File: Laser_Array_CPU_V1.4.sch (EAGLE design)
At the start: 71 parts, among them IC1 PIC24FJ64GA004, J1 MA16-2, J3 22-23-2021, J4 22-23-2021, J8 22-23-2021, U1 MAX6817, U2 LP2985-28DBVTE4, U4 LP2985-50DBVR, X1 22-23-2031, X2 22-23-2041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

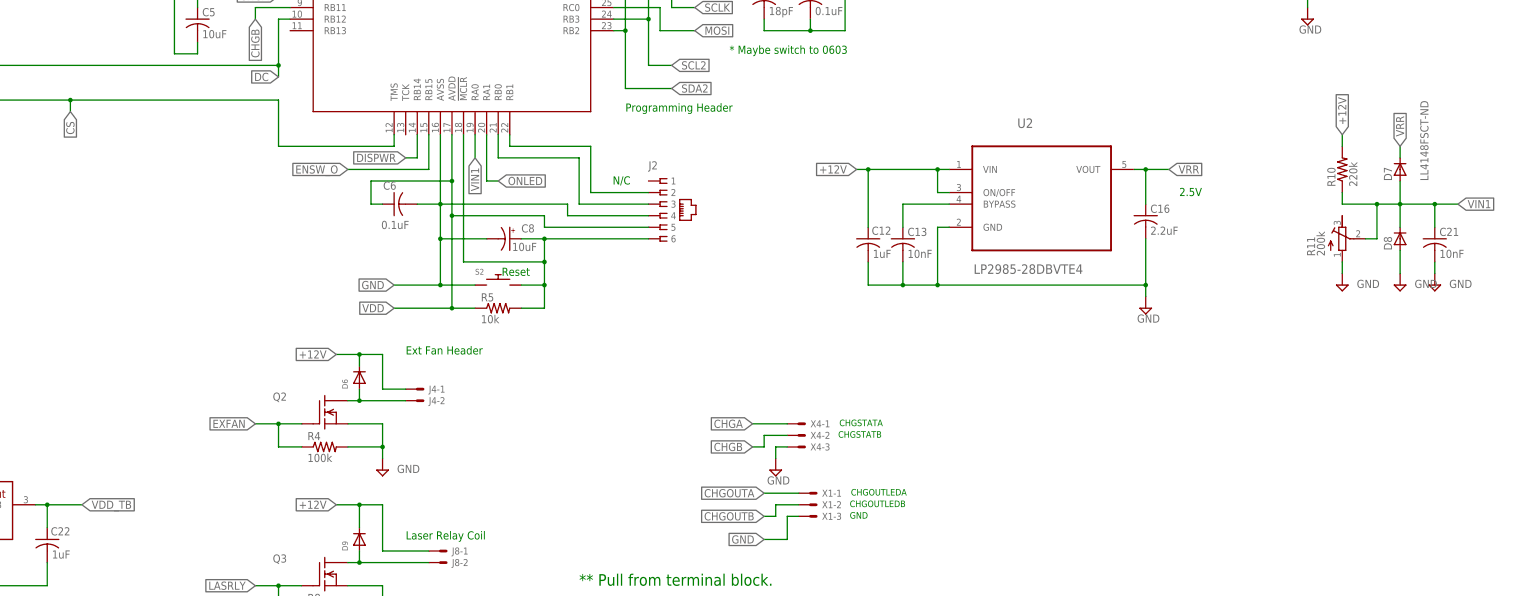
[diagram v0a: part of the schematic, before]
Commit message: Finished Laser_Array next versions, all three boards including revised charger board
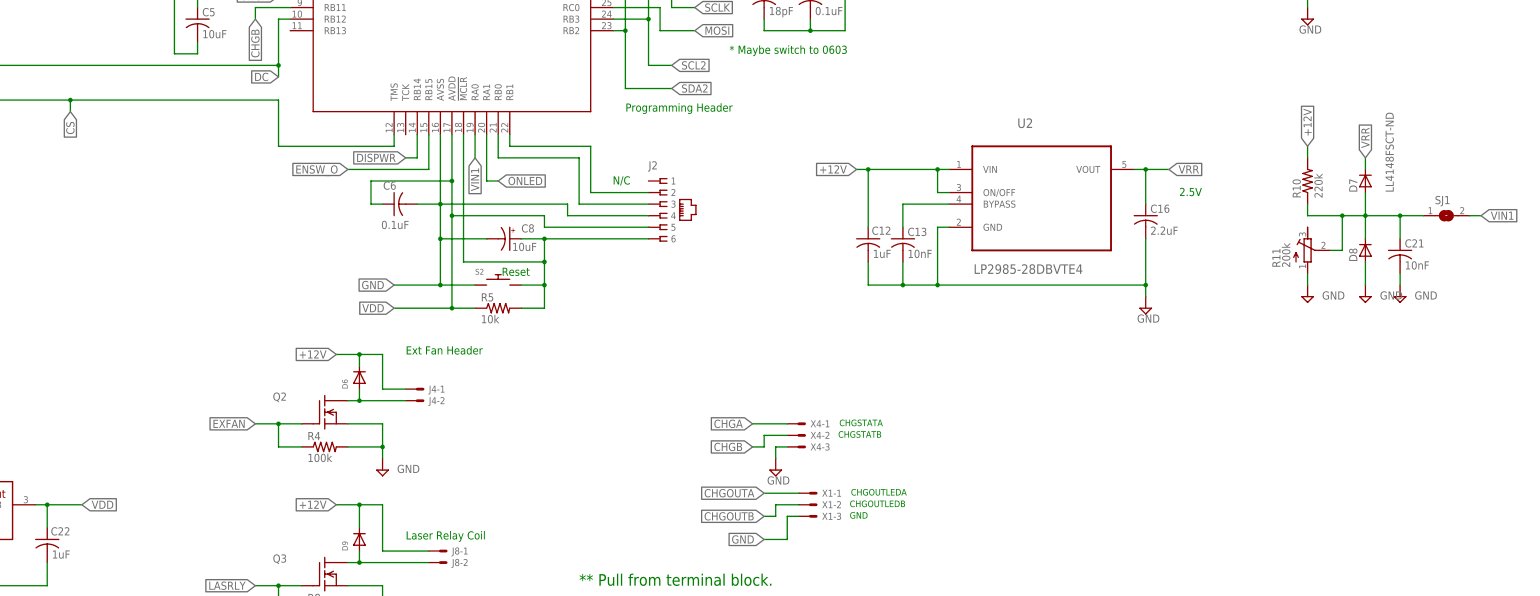
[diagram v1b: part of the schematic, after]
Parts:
- added SJ1: (no value), jumper:SJ
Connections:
- removed net N$3: C22.1, U3.P$3
- net VDD: now also C22.1, U3.P$3
- net VIN1: now also SJ1.1, SJ1.2
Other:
- moved on the sheet: C21, D7, D8, R10, R11
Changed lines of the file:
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@@
 </variantdefs>
 <classes>
-<class number="0" name="default" width="0.254" drill="0.508">
+<class number="0" name="default" width="0.1016" drill="0.508">
 <clearance class="0" value="0.2032"/>
 </class>
@@
 <part name="C23" library="rcl" deviceset="C-US" device="C0805" value="4.7uF"/>
 <part name="SUPPLY6" library="supply2" deviceset="GND" device=""/>
+<part name="SJ1" library="jumper" deviceset="SJ" device=""/>
 </parts>
 <sheets>
@@
 <attribute name="VALUE" x="168.656" y="-1.651" size="1.778" layer="96"/>
 </instance>
-<instance part="R10" gate="G$1" x="210.82" y="12.7" smashed="yes" rot="R90">
-<attribute name="NAME" x="209.3214" y="8.89" size="1.778" layer="95" rot="R90"/>
-<attribute name="VALUE" x="214.122" y="8.89" size="1.778" layer="96" rot="R90"/>
-</instance>
-<instance part="SUPPLY9" gate="GND" x="210.82" y="-12.7" smashed="yes">
-<attribute name="VALUE" x="213.995" y="-13.335" size="1.778" layer="96"/>
-</instance>
-<instance part="C21" gate="G$1" x="231.14" y="-2.54" smashed="yes">
-<attribute name="NAME" x="232.156" y="-1.905" size="1.778" layer="95"/>
-<attribute name="VALUE" x="232.156" y="-6.731" size="1.778" layer="96"/>
-</instance>
-<instance part="SUPPLY12" gate="GND" x="231.14" y="-12.7" smashed="yes">
-<attribute name="VALUE" x="234.315" y="-13.335" size="1.778" layer="96"/>
-</instance>
-<instance part="D7" gate="G$1" x="223.52" y="12.7" smashed="yes" rot="R90">
-<attribute name="NAME" x="221.742" y="10.16" size="1.778" layer="95" rot="R90"/>
-<attribute name="VALUE" x="229.743" y="10.16" size="1.778" layer="96" rot="R90"/>
-</instance>
-<instance part="D8" gate="G$1" x="223.52" y="-2.54" smashed="yes" rot="R90">
-<attribute name="NAME" x="221.742" y="-5.08" size="1.778" layer="95" rot="R90"/>
-</instance>
-<instance part="SUPPLY10" gate="GND" x="223.52" y="-12.7" smashed="yes">
-<attribute name="VALUE" x="226.695" y="-13.335" size="1.778" layer="96"/>
-</instance>
-<instance part="R11" gate="G$1" x="210.82" y="-2.54"/>
+<instance part="R10" gate="G$1" x="203.2" y="10.16" smashed="yes" rot="R90">
+<attribute name="NAME" x="201.7014" y="6.35" size="1.778" layer="95" rot="R90"/>
+<attribute name="VALUE" x="206.502" y="6.35" size="1.778" layer="96" rot="R90"/>
+</instance>
+<instance part="SUPPLY9" gate="GND" x="203.2" y="-15.24" smashed="yes">
+<attribute name="VALUE" x="206.375" y="-15.875" size="1.778" layer="96"/>
+</instance>
+<instance part="C21" gate="G$1" x="223.52" y="-5.08" smashed="yes">
+<attribute name="NAME" x="224.536" y="-4.445" size="1.778" layer="95"/>
+<attribute name="VALUE" x="224.536" y="-9.271" size="1.778" layer="96"/>
+</instance>
+<instance part="SUPPLY12" gate="GND" x="223.52" y="-15.24" smashed="yes">
+<attribute name="VALUE" x="226.695" y="-15.875" size="1.778" layer="96"/>
+</instance>
+<instance part="D7" gate="G$1" x="215.9" y="10.16" smashed="yes" rot="R90">
+<attribute name="NAME" x="214.122" y="7.62" size="1.778" layer="95" rot="R90"/>
+<attribute name="VALUE" x="222.123" y="7.62" size="1.778" layer="96" rot="R90"/>
+</instance>
+<instance part="D8" gate="G$1" x="215.9" y="-5.08" smashed="yes" rot="R90">
+<attribute name="NAME" x="214.122" y="-7.62" size="1.778" layer="95" rot="R90"/>
+</instance>
+<instance part="SUPPLY10" gate="GND" x="215.9" y="-15.24" smashed="yes">
+<attribute name="VALUE" x="219.075" y="-15.875" size="1.778" layer="96"/>
+</instance>
+<instance part="R11" gate="G$1" x="203.2" y="-5.08"/>
 <instance part="R13" gate="G$1" x="200.66" y="76.2" smashed="yes" rot="R90">
 <attribute name="NAME" x="199.1614" y="72.39" size="1.778" layer="95" rot="R90"/>
@@
 </instance>
 <instance part="SUPPLY6" gate="GND" x="-88.9" y="-86.36"/>
+<instance part="SJ1" gate="1" x="233.68" y="2.54"/>
 </instances>
 <busses>
@@
 <wire x1="-139.7" y1="78.74" x2="-134.62" y2="78.74" width="0.1524" layer="91"/>
 </segment>
+<segment>
+<pinref part="U3" gate="G$1" pin="P$3"/>
+<wire x1="-76.2" y1="-60.96" x2="-73.66" y2="-60.96" width="0.1524" layer="91"/>
+<pinref part="C22" gate="G$1" pin="1"/>
+<wire x1="-73.66" y1="-60.96" x2="-66.04" y2="-60.96" width="0.1524" layer="91"/>
+<wire x1="-73.66" y1="-66.04" x2="-73.66" y2="-60.96" width="0.1524" layer="91"/>
+<junction x="-73.66" y="-60.96"/>
+<label x="-66.04" y="-60.96" size="1.778" layer="95" xref="yes"/>
+</segment>
 </net>
 <net name="+12V" class="0">
@@
 <segment>
 <pinref part="R10" gate="G$1" pin="2"/>
-<wire x1="210.82" y1="17.78" x2="210.82" y2="20.32" width="0.1524" layer="91"/>
-<label x="210.82" y="20.32" size="1.778" layer="95" rot="R90" xref="yes"/>
+<wire x1="203.2" y1="15.24" x2="203.2" y2="17.78" width="0.1524" layer="91"/>
+<label x="203.2" y="17.78" size="1.778" layer="95" rot="R90" xref="yes"/>
 </segment>
 <segment>
@@
 <segment>
 <pinref part="SUPPLY9" gate="GND" pin="GND"/>
-<wire x1="210.82" y1="-7.62" x2="210.82" y2="-10.16" width="0.1524" layer="91"/>
+<wire x1="203.2" y1="-10.16" x2="203.2" y2="-12.7" width="0.1524" layer="91"/>
 <pinref part="R11" gate="G$1" pin="A"/>
 </segment>
@@
 <pinref part="SUPPLY12" gate="GND" pin="GND"/>
 <pinref part="C21" gate="G$1" pin="2"/>
-<wire x1="231.14" y1="-10.16" x2="231.14" y2="-7.62" width="0.1524" layer="91"/>
+<wire x1="223.52" y1="-12.7" x2="223.52" y2="-10.16" width="0.1524" layer="91"/>
 </segment>
 <segment>
 <pinref part="SUPPLY10" gate="GND" pin="GND"/>
 <pinref part="D8" gate="G$1" pin="A"/>
-<wire x1="223.52" y1="-10.16" x2="223.52" y2="-5.08" width="0.1524" layer="91"/>
+<wire x1="215.9" y1="-12.7" x2="215.9" y2="-7.62" width="0.1524" layer="91"/>
 </segment>
 <segment>
@@
 <segment>
 <pinref part="D7" gate="G$1" pin="C"/>
-<wire x1="223.52" y1="15.24" x2="223.52" y2="17.78" width="0.1524" layer="91"/>
-<label x="223.52" y="17.78" size="1.778" layer="95" rot="R90" xref="yes"/>
+<wire x1="215.9" y1="12.7" x2="215.9" y2="15.24" width="0.1524" layer="91"/>
+<label x="215.9" y="15.24" size="1.778" layer="95" rot="R90" xref="yes"/>
 </segment>
 </net>
@@
 <segment>
 <pinref part="R10" gate="G$1" pin="1"/>
-<wire x1="210.82" y1="7.62" x2="210.82" y2="5.08" width="0.1524" layer="91"/>
+<wire x1="203.2" y1="5.08" x2="203.2" y2="2.54" width="0.1524" layer="91"/>
 <pinref part="C21" gate="G$1" pin="1"/>
-<wire x1="231.14" y1="0" x2="231.14" y2="5.08" width="0.1524" layer="91"/>
-<wire x1="231.14" y1="5.08" x2="223.52" y2="5.08" width="0.1524" layer="91"/>
+<wire x1="223.52" y1="-2.54" x2="223.52" y2="2.54" width="0.1524" layer="91"/>
+<wire x1="223.52" y1="2.54" x2="215.9" y2="2.54" width="0.1524" layer="91"/>
 <pinref part="D8" gate="G$1" pin="C"/>
-<wire x1="223.52" y1="5.08" x2="218.44" y2="5.08" width="0.1524" layer="91"/>
-<wire x1="218.44" y1="5.08" x2="210.82" y2="5.08" width="0.1524" layer="91"/>
-<wire x1="223.52" y1="0" x2="223.52" y2="5.08" width="0.1524" layer="91"/>
-<junction x="223.52" y="5.08"/>
+<wire x1="215.9" y1="2.54" x2="210.82" y2="2.54" width="0.1524" layer="91"/>
+<wire x1="210.82" y1="2.54" x2="203.2" y2="2.54" width="0.1524" layer="91"/>
+<wire x1="215.9" y1="-2.54" x2="215.9" y2="2.54" width="0.1524" layer="91"/>
+<junction x="215.9" y="2.54"/>
 <pinref part="D7" gate="G$1" pin="A"/>
-<wire x1="223.52" y1="10.16" x2="223.52" y2="5.08" width="0.1524" layer="91"/>
-<junction x="231.14" y="5.08"/>
-<label x="236.22" y="5.08" size="1.778" layer="95" xref="yes"/>
-<wire x1="236.22" y1="5.08" x2="231.14" y2="5.08" width="0.1524" layer="91"/>
+<wire x1="215.9" y1="7.62" x2="215.9" y2="2.54" width="0.1524" layer="91"/>
+<junction x="223.52" y="2.54"/>
+<wire x1="228.6" y1="2.54" x2="223.52" y2="2.54" width="0.1524" layer="91"/>
 <pinref part="R11" gate="G$1" pin="S"/>
-<wire x1="215.9" y1="-2.54" x2="218.44" y2="-2.54" width="0.1524" layer="91"/>
-<wire x1="218.44" y1="-2.54" x2="218.44" y2="5.08" width="0.1524" layer="91"/>
-<junction x="218.44" y="5.08"/>
+<wire x1="208.28" y1="-5.08" x2="210.82" y2="-5.08" width="0.1524" layer="91"/>
+<wire x1="210.82" y1="-5.08" x2="210.82" y2="2.54" width="0.1524" layer="91"/>
+<junction x="210.82" y="2.54"/>
+<pinref part="SJ1" gate="1" pin="1"/>
 </segment>
 <segment>
@@
 <wire x1="20.32" y1="20.32" x2="20.32" y2="15.24" width="0.1524" layer="91"/>
 <label x="20.32" y="15.24" size="1.778" layer="95" rot="R270" xref="yes"/>
+</segment>
+<segment>
+<pinref part="SJ1" gate="1" pin="2"/>
+<wire x1="238.76" y1="2.54" x2="241.3" y2="2.54" width="0.1524" layer="91"/>
+<label x="241.3" y="2.54" size="1.778" layer="95" xref="yes"/>
 </segment>
 </net>
@@
 </segment>
 </net>
-<net name="N$3" class="0">
-<segment>
-<pinref part="U3" gate="G$1" pin="P$3"/>
-<wire x1="-76.2" y1="-60.96" x2="-73.66" y2="-60.96" width="0.1524" layer="91"/>
-<pinref part="C22" gate="G$1" pin="1"/>
-<wire x1="-73.66" y1="-60.96" x2="-66.04" y2="-60.96" width="0.1524" layer="91"/>
-<wire x1="-73.66" y1="-66.04" x2="-73.66" y2="-60.96" width="0.1524" layer="91"/>
-<junction x="-73.66" y="-60.96"/>
-</segment>
-</net>
 <net name="VDD_TB" class="0">
 <segment>
-<label x="-66.04" y="-60.96" size="1.778" layer="95" xref="yes"/>
 <wire x1="-124.46" y1="-60.96" x2="-116.84" y2="-60.96" width="0.1524" layer="91"/>
 <pinref part="R3" gate="G$1" pin="2"/>
